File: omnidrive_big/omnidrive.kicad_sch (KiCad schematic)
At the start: 85 parts, among them J1 AudioJack3, J6 AudioJack2, U1 TL072, U2 TL072

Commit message: Fix omnidrive schematic; other things too
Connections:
- net at C11.1, J_FILT_2.1 (Pin_1), SW_FILTER_2.3 (C): now also R5.2, R6.2, U1.1
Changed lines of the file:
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@@
+	)
+	(junction
+		(at 124.46 55.88)
+		(diameter 0)
+		(color 0 0 0 0)
 	)
 	(junction
@@
 	)
 	(junction
+		(at 124.46 36.83)
+		(diameter 0)
+		(color 0 0 0 0)
+	)
+	(junction
 		(at 175.26 87.63)
 		(diameter 0)
@@
 	(wire
 		(pts
-			(xy 167.64 55.88) (xy 72.39 55.88)
+			(xy 167.64 55.88) (xy 124.46 55.88)
 		)
 		(stroke
@@
 	(wire
 		(pts
+			(xy 124.46 36.83) (xy 124.46 55.88)
+		)
+		(stroke
+			(width 0)
+			(type default)
+		)
+	)
+	(wire
+		(pts
 			(xy 69.85 30.48) (xy 69.85 16.51)
 		)
@@
 		)
 		(stroke
+			(width 0)
+			(type default)
+		)
+	)
+	(wire
+		(pts
+			(xy 124.46 55.88) (xy 72.39 55.88)
+		)
+		(stroke

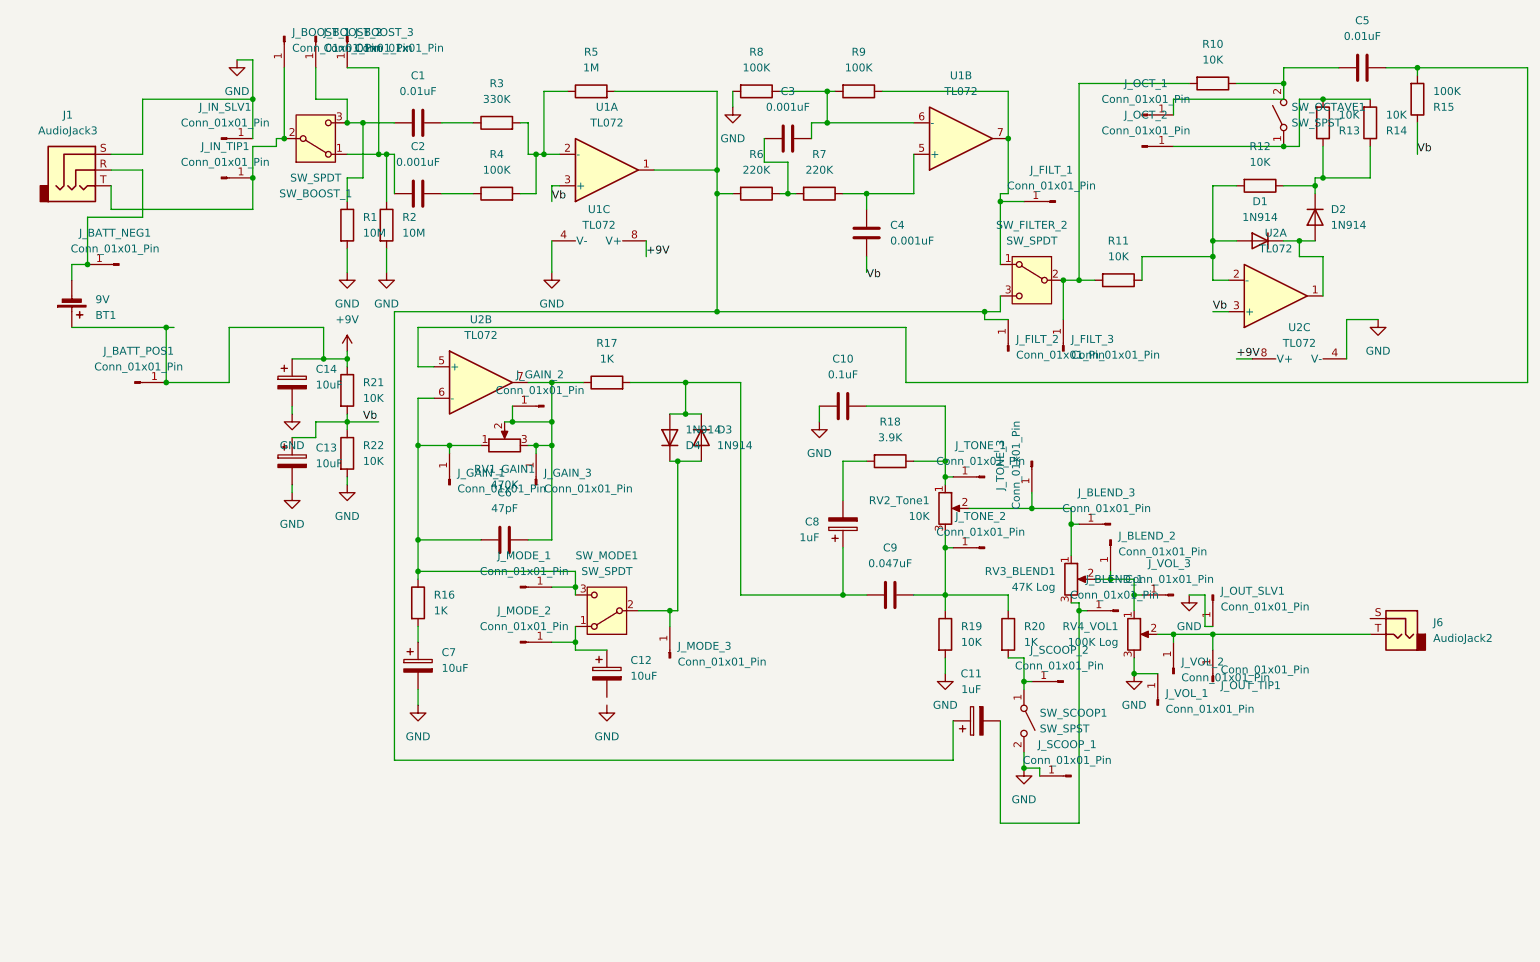
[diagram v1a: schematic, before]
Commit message: my own layout, components placed
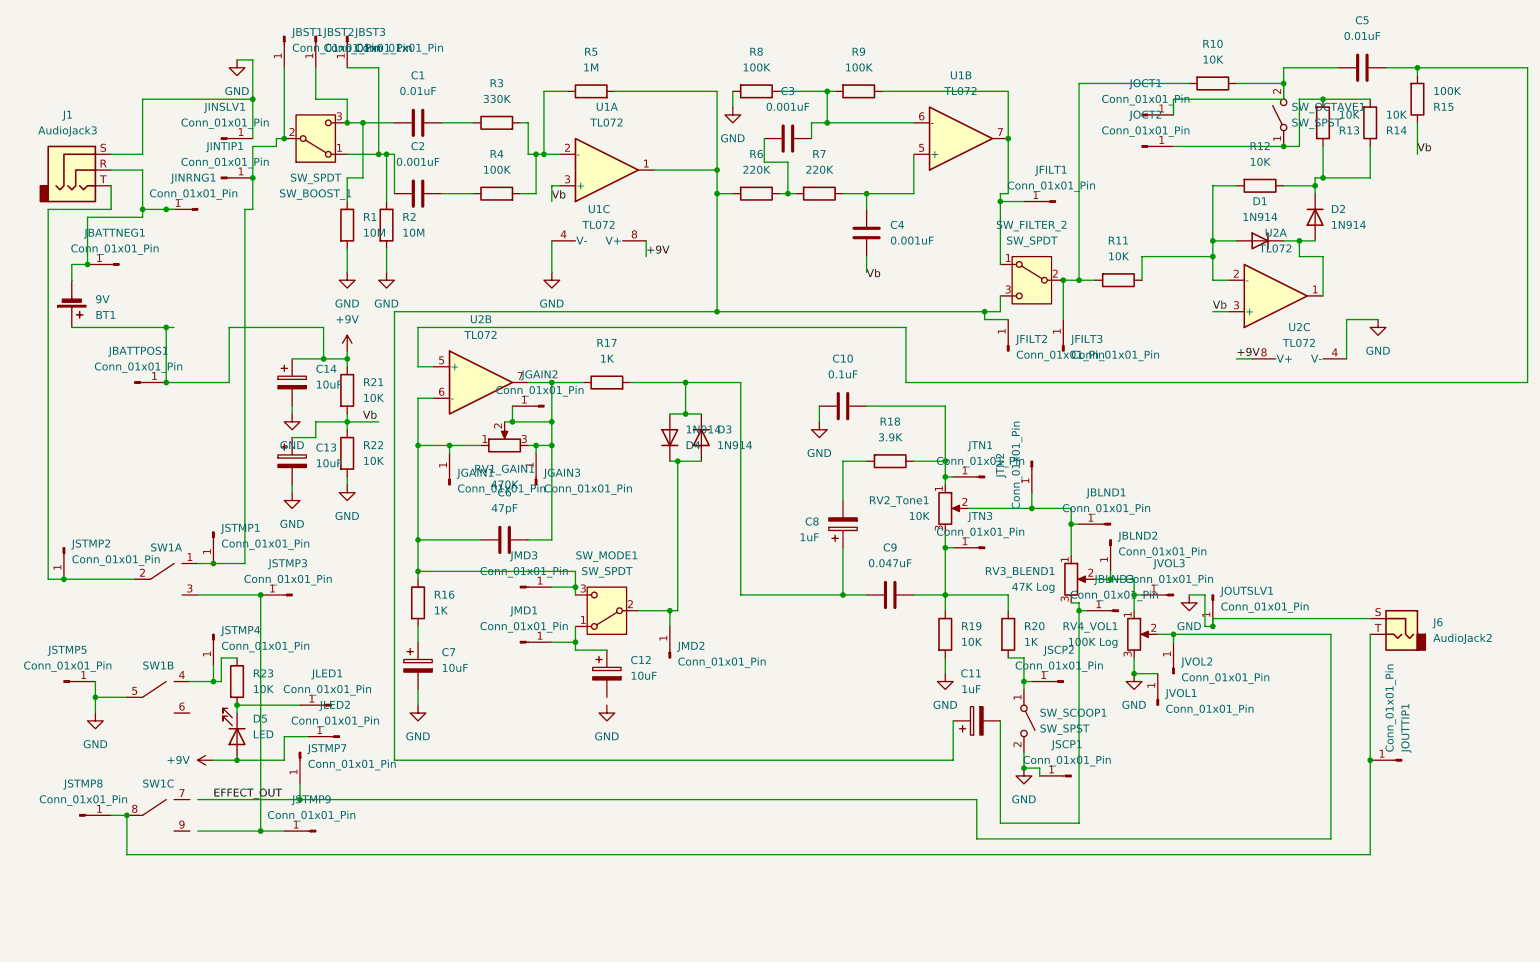
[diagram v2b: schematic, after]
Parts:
- added D5: LED, symbol Device:LED
- added JINRNG1, JLED1, JLED2, JSTMP1, JSTMP2, JSTMP3, JSTMP4, JSTMP5, JSTMP7, JSTMP8, JSTMP9: Conn_01x01_Pin, Connector_PinSocket_2.54mm:PinSocket_1x01_P2.54mm_Vertical, symbol Connector:Conn_01x01_Pin
- added R23: 10K, Resistor_THT:R_Axial_DIN0207_L6.3mm_D2.5mm_P7.62mm_Horizontal, symbol Device:R
- added SW1: (no value), symbol ohmify-switches:Switch_3PDT
- renumbered J_BATT_NEG1 to JBATTNEG1, J_BATT_POS1 to JBATTPOS1, J_BLEND_3 to JBLND1, J_BLEND_2 to JBLND2, J_BLEND_1 to JBLND3, J_BOOST_1 to JBST1, J_BOOST_2 to JBST2, J_BOOST_3 to JBST3, J_FILT_1 to JFILT1, J_FILT_2 to JFILT2, J_FILT_3 to JFILT3, J_GAIN_1 to JGAIN1, J_GAIN_2 to JGAIN2, J_GAIN_3 to JGAIN3, J_IN_SLV1 to JINSLV1, J_IN_TIP1 to JINTIP1, J_MODE_2 to JMD1, J_MODE_3 to JMD2, J_MODE_1 to JMD3, J_OCT_1 to JOCT1, J_OCT_2 to JOCT2, J_OUT_SLV1 to JOUTSLV1, J_OUT_TIP1 to JOUTTIP1, J_SCOOP_1 to JSCP1, J_SCOOP_2 to JSCP2, J_TONE_1 to JTN1, J_TONE_3 to JTN2, J_TONE_2 to JTN3, J_VOL_1 to JVOL1, J_VOL_2 to JVOL2, J_VOL_3 to JVOL3
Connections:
- net +9V: now also D5.2 (A), JLED2.1 (Pin_1)
- net GND: now also J6.S, JSTMP5.1 (Pin_1), SW1.5
- net at J6.T, JOUTTIP1.1 (Pin_1): now also JSTMP8.1 (Pin_1), SW1.8; no longer JVOL2.1 (Pin_1), RV4_VOL1.2
- net at BT1.2 (-), J1.R, JBATTNEG1.1 (Pin_1): now also JINRNG1.1 (Pin_1)
- net at JBST1.1 (Pin_1), JINTIP1.1 (Pin_1), SW_BOOST_1.2 (B): now also JSTMP1.1 (Pin_1), SW1.1; no longer J1.T
- new net: J1.T, JSTMP2.1 (Pin_1), SW1.2
- new net: JSTMP3.1 (Pin_1), JSTMP9.1 (Pin_1), SW1.3
- new net: JSTMP4.1 (Pin_1), R23.1, SW1.4
- new net: D5.1 (K), JLED1.1 (Pin_1), R23.2
- new net EFFECT_OUT: JSTMP7.1 (Pin_1), JVOL2.1 (Pin_1), RV4_VOL1.2
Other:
- moved on the sheet: JOUTTIP1

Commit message: placed + routed everything except ground plane
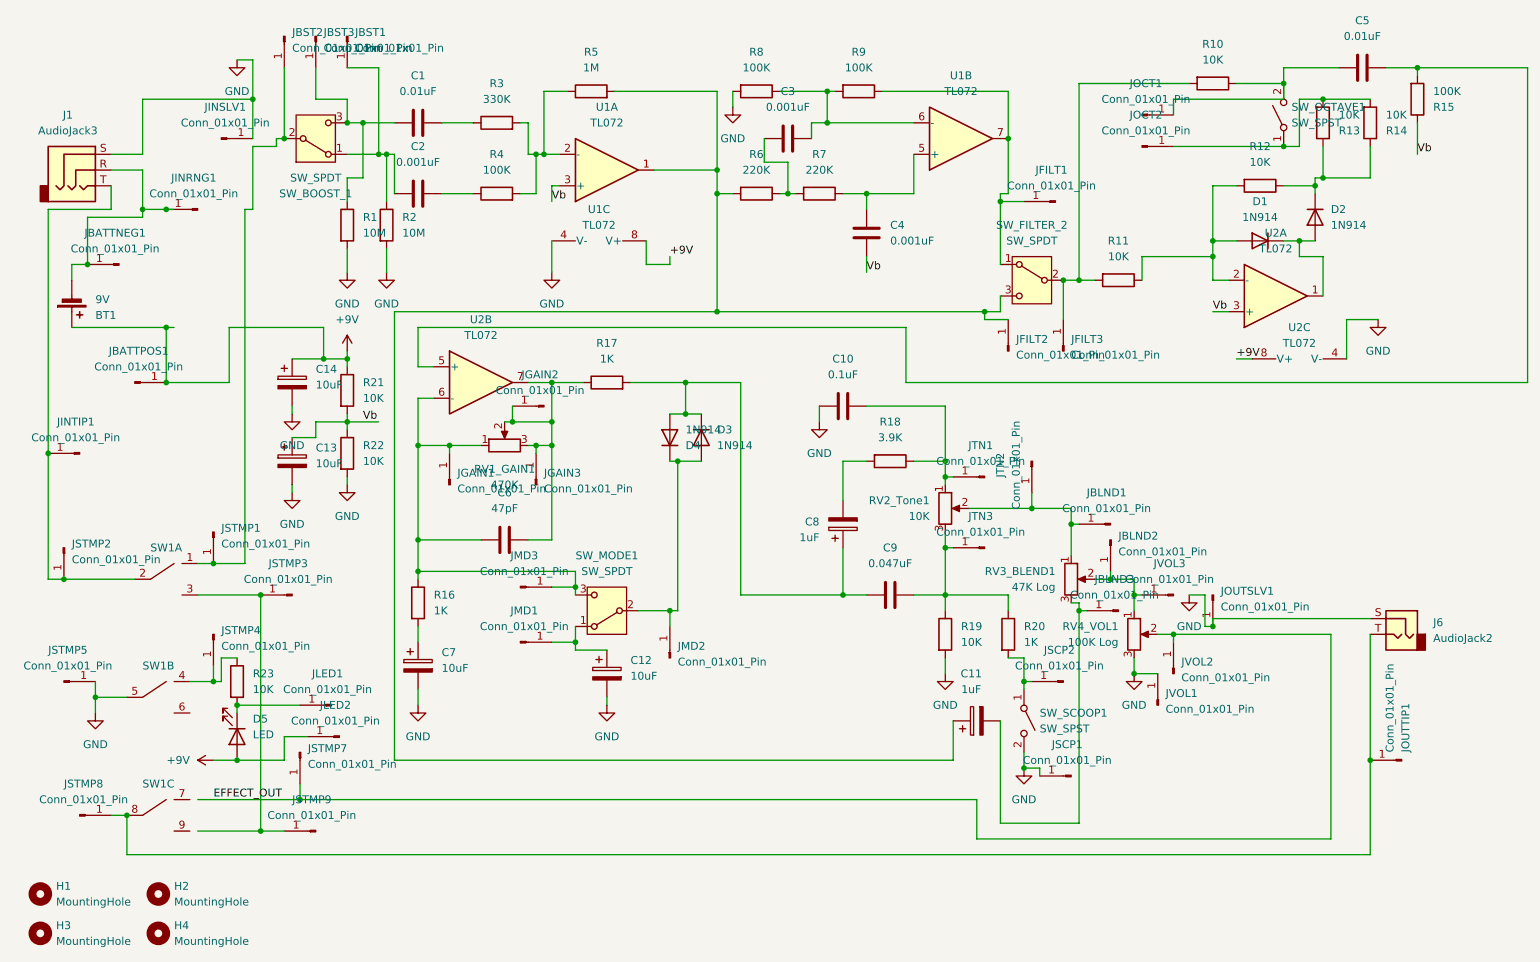
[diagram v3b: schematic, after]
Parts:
- added H1, H2, H3, H4: MountingHole, MountingHole:MountingHole_3.2mm_M3, symbol Mechanical:MountingHole
- renumbered JBST3 to JBST1, JBST1 to JBST2, JBST2 to JBST3
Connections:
- net GND: now also C12.2
- net Vb: now also C4.1
- net at JBST2.1 (Pin_1), JSTMP1.1 (Pin_1), SW1.1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: no longer JINTIP1.1 (Pin_1)
- net at J1.T, JSTMP2.1 (Pin_1), SW1.2: now also JINTIP1.1 (Pin_1)
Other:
- moved on the sheet: JINTIP1
